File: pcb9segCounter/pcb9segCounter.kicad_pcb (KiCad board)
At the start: 2 copper layers, 10 parts

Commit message: Making progress, figuring out microcontroller interfacing
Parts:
- removed the D1 at (148.2, 54.6)
- added C1: 0.1u, Capacitor_SMD:C_0805_2012Metric, F.Cu at (64.0, 142.5)
- added D10: ~, customParts:1x1mm SMD RGB LED, F.Cu at (103.6, 49.3)
- added D11: ~, customParts:1x1mm SMD RGB LED, F.Cu at (115.5, 60.0)
- added D12: ~, customParts:1x1mm SMD RGB LED, F.Cu at (117.6, 79.1)
- added D13: ~, customParts:1x1mm SMD RGB LED, F.Cu at (107.3, 90.8)
- added D14: ~, customParts:1x1mm SMD RGB LED, F.Cu at (94.8, 80.1)
- added D15: ~, customParts:1x1mm SMD RGB LED, F.Cu at (92.8, 60.7)
- added D16: ~, customParts:1x1mm SMD RGB LED, F.Cu at (100.7, 62.5)
- added D17: ~, customParts:1x1mm SMD RGB LED, F.Cu at (103.3, 67.2)
- added D18: ~, customParts:1x1mm SMD RGB LED, F.Cu at (103.6, 80.3)
- added D19: ~, customParts:1x1mm SMD RGB LED, F.Cu at (131.5, 49.3)
- added D20: ~, customParts:1x1mm SMD RGB LED, F.Cu at (143.4, 60.0)
- added D21: ~, customParts:1x1mm SMD RGB LED, F.Cu at (145.6, 79.1)
- added D22: ~, customParts:1x1mm SMD RGB LED, F.Cu at (135.2, 90.8)
- added D23: ~, customParts:1x1mm SMD RGB LED, F.Cu at (122.7, 80.1)
- added D24: ~, customParts:1x1mm SMD RGB LED, F.Cu at (120.8, 60.7)
- added D25: ~, customParts:1x1mm SMD RGB LED, F.Cu at (128.7, 62.5)
- added D26: ~, customParts:1x1mm SMD RGB LED, F.Cu at (131.2, 67.2)
- added D27: ~, customParts:1x1mm SMD RGB LED, F.Cu at (131.5, 80.3)
- added D28: ~, customParts:1x1mm SMD RGB LED, F.Cu at (159.4, 49.3)
- added D29: ~, customParts:1x1mm SMD RGB LED, F.Cu at (171.4, 60.0)
- added D30: ~, customParts:1x1mm SMD RGB LED, F.Cu at (173.5, 79.1)
- added D31: ~, customParts:1x1mm SMD RGB LED, F.Cu at (163.2, 90.8)
- added D32: ~, customParts:1x1mm SMD RGB LED, F.Cu at (150.7, 80.1)
- added D33: ~, customParts:1x1mm SMD RGB LED, F.Cu at (148.7, 60.7)
- added D34: ~, customParts:1x1mm SMD RGB LED, F.Cu at (156.6, 62.5)
- added D35: ~, customParts:1x1mm SMD RGB LED, F.Cu at (159.1, 67.2)
- added D36: ~, customParts:1x1mm SMD RGB LED, F.Cu at (159.4, 80.3)
- added J1: SAO, Connector_PinHeader_2.54mm:PinHeader_2x03_P2.54mm_Vertical, F.Cu at (73.3, 130.7)
- added J2: AVR-ISP-6, Connector_PinHeader_2.54mm:PinHeader_2x03_P2.54mm_Vertical, F.Cu at (64.1, 130.7)
- added R1: 1k, Resistor_SMD:R_0805_2012Metric_Pad1.20x1.40mm_HandSolder, F.Cu at (64.1, 139.5)
- added R2: 1k, Resistor_SMD:R_0805_2012Metric, F.Cu at (55.5, 140.2)
- added R3: 1k, Resistor_SMD:R_0805_2012Metric, F.Cu at (55.5, 143.1)
- added S1: ~, customParts:9 Segment 38x19x3, B.Cu at (88.9, 50.8)
- added S2: ~, customParts:9 Segment 38x19x3, B.Cu at (116.8, 50.8)
- added S3: ~, customParts:9 Segment 38x19x3, B.Cu at (144.8, 50.8)
- added S4: ~, customParts:9 Segment 38x19x3, B.Cu at (172.7, 50.8)
- added U1: ATtiny84A-SS, Package_SO:SOIC-14_3.9x8.7mm_P1.27mm, F.Cu at (57.5, 133.6)
- moved D7 60.3 mm to (72.8, 62.5)
- moved D8 60.2 mm to (75.3, 67.2)
- moved D4 59.4 mm to (79.3, 90.8)
- moved D2 59.4 mm to (87.5, 60.0)
- moved D5 59.4 mm to (66.9, 80.1)
- moved D1 59.4 mm to (75.6, 49.3)
- moved D3 59.4 mm to (89.7, 79.1)
- moved D6 59.4 mm to (64.9, 60.7)
- moved D9 59.4 mm to (75.6, 80.3)
- renumbered D2 to D1, D3 to D2, D4 to D3, D5 to D4, D6 to D5, D7 to D6, D8 to D7, D9 to D8, D10 to D9
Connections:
- net /pcb9SegDigit/pwr+ renamed +5V
- net /pcb9SegDigit/pwr- renamed GND
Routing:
- net GND: track 79.1 -> 646.1 mm
- net +5V: track 73.7 -> 606.5 mm
- net /pcb9SegDigit2/DOUT: track 0.00 -> 68.7 mm, vias 0 -> 2
- net /pcb9SegDigit1/DOUT: track 0.00 -> 68.7 mm, vias 0 -> 2
- net /pcb9SegDigit/DOUT: track 0.00 -> 68.7 mm, vias 0 -> 2
- net Net-(D15-DOUT): track 0.00 -> 26.3 mm
- net Net-(D24-DOUT): track 0.00 -> 26.3 mm
- net Net-(D33-DOUT): track 0.00 -> 26.3 mm
- net Net-(D21-DOUT): track 0.00 -> 20.2 mm
- net Net-(D12-DOUT): track 0.00 -> 20.2 mm
- net Net-(D30-DOUT): track 0.00 -> 20.2 mm
- net Net-(D3-DOUT): track 0.00 -> 20.2 mm
- net Net-(D28-DOUT): track 0.00 -> 19.4 mm
- net Net-(D19-DOUT): track 0.00 -> 19.4 mm
- net Net-(D10-DOUT): track 0.00 -> 19.4 mm
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
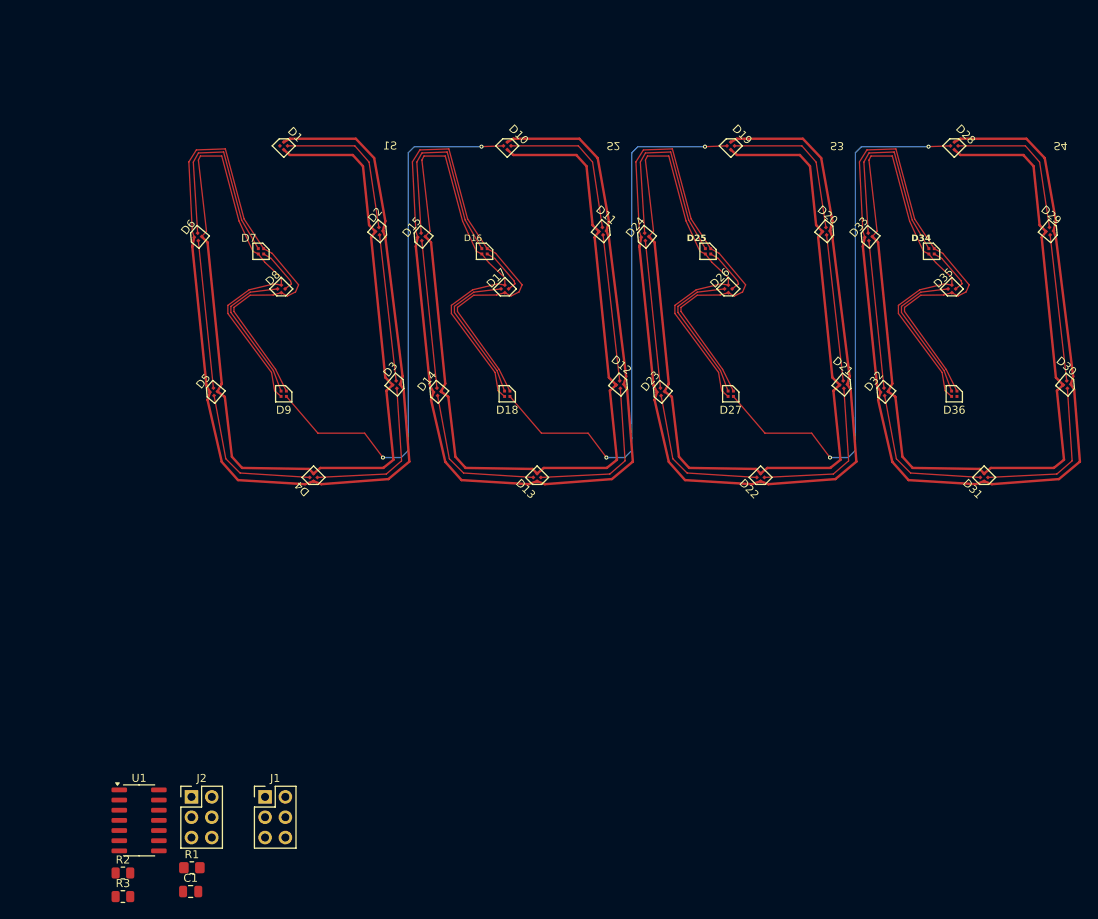
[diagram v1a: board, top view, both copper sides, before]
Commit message: Schematic looks good, going to branch to reduce the number of digits from 4 to 2
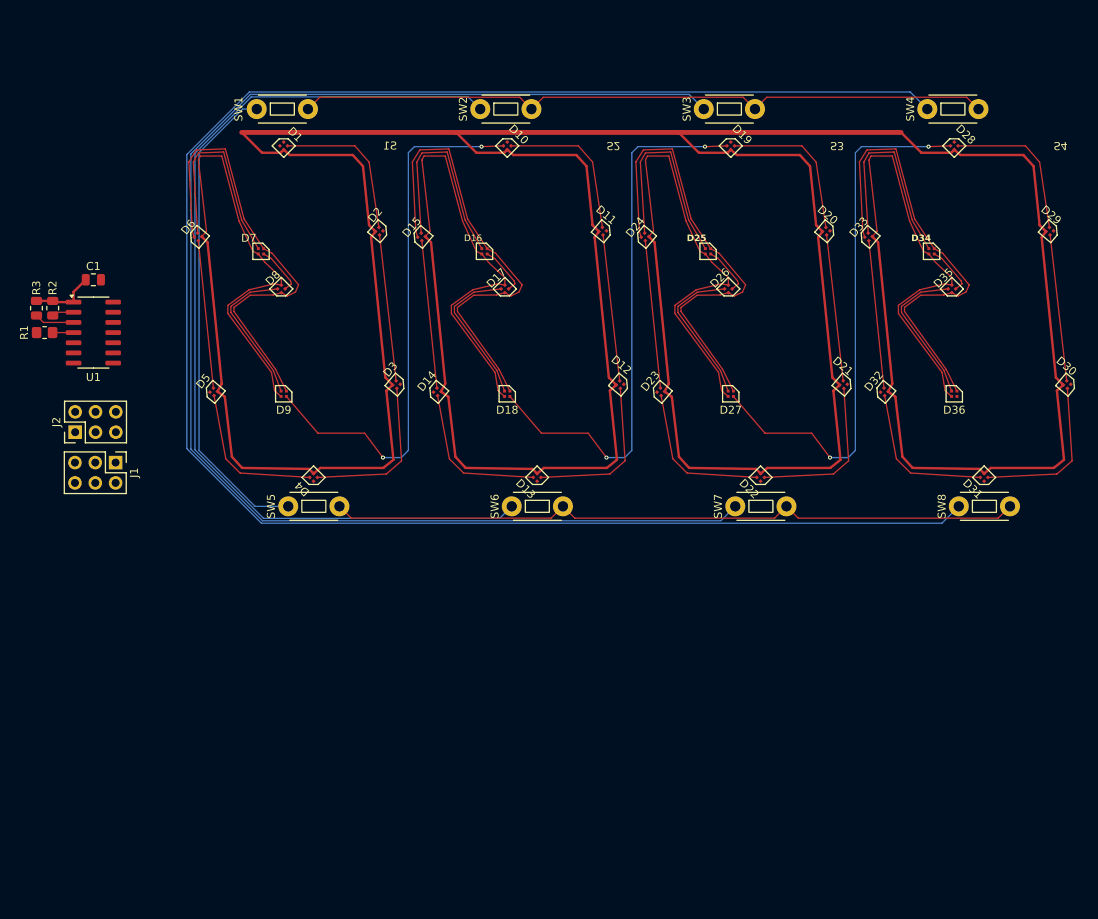
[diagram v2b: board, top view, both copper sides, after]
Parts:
- added SW1: ~, customParts:PTS636 SK43 LFS, F.Cu at (75.4, 44.7)
- added SW2: ~, customParts:PTS636 SK43 LFS, F.Cu at (103.4, 44.7)
- added SW3: ~, customParts:PTS636 SK43 LFS, F.Cu at (131.3, 44.7)
- added SW4: ~, customParts:PTS636 SK43 LFS, F.Cu at (159.3, 44.7)
- added SW5: ~, customParts:PTS636 SK43 LFS, F.Cu at (79.4, 94.4)
- added SW6: ~, customParts:PTS636 SK43 LFS, F.Cu at (107.3, 94.4)
- added SW7: ~, customParts:PTS636 SK43 LFS, F.Cu at (135.3, 94.4)
- added SW8: ~, customParts:PTS636 SK43 LFS, F.Cu at (163.2, 94.4)
- moved C1 77.4 mm to (51.8, 66.0)
- moved R3 74.3 mm to (44.7, 69.6), turned to -90 degrees
- moved R2 71.1 mm to (46.7, 69.6), turned to -90 degrees
- moved R1 69.4 mm to (45.7, 72.6)
- moved U1 61.2 mm to (51.8, 72.6)
- moved J2 47.8 mm to (49.5, 85.1), turned to 90 degrees
- moved J1 45.8 mm to (54.6, 88.9), turned to -90 degrees
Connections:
- J2 pad 3: /uC/SCK -> SCL
- J2 pad 4: /uC/MOSI -> SDA
- U1 pad 6: unconnected-(U1-PA7-Pad6) -> GP1
- U1 pad 7: /uC/MOSI -> SDA
- U1 pad 9: /uC/SCK -> SCL
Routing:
- net GND: track 646.1 -> 226.5 mm
- net /uC/tho: track 0.00 -> 234.7 mm
- net /uC/hnd: track 0.00 -> 177.4 mm
- net +5V: track 606.5 -> 726.7 mm
- net /uC/ten: track 0.00 -> 120.0 mm
- net /uC/dec: track 0.00 -> 92.5 mm
- net /uC/inc: track 0.00 -> 90.3 mm
- net /uC/one: track 0.00 -> 60.7 mm
- net /uC/RST: track 0.00 -> 2.62 mm

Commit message: reduced to 2 digits, added capacitors
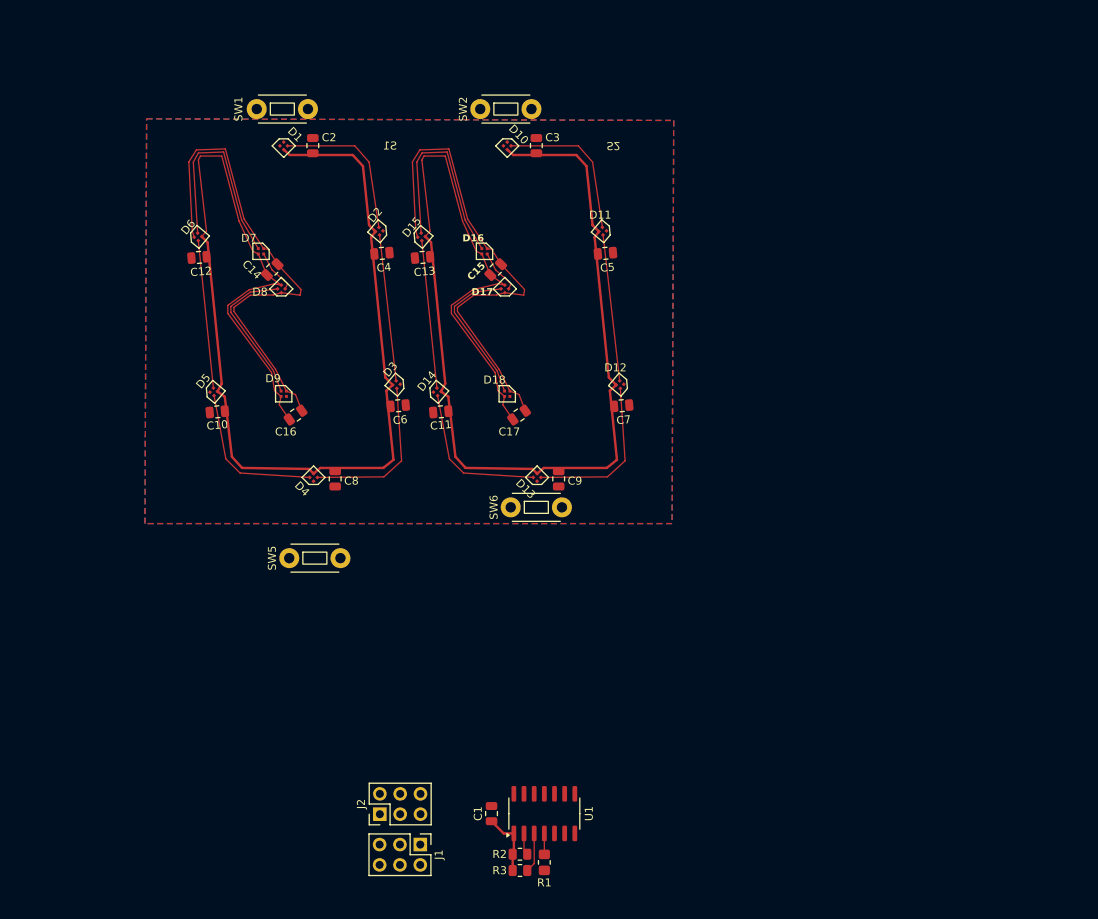
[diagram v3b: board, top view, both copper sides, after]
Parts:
- removed D19, D20, D21, D22, D23, D24, D25, D26, D27, D28, D29, D30, D31, D32, D33, D34, D35, D36: ~, customParts:1x1mm SMD RGB LED
- removed S3, S4: ~, customParts:9 Segment 38x19x3
- removed SW3, SW4, SW7, SW8: ~, customParts:PTS636 SK43 LFS
- added C10: 0.1u, Capacitor_SMD:C_0805_2012Metric, F.Cu at (67.3, 82.5)
- added C11: 0.1u, Capacitor_SMD:C_0805_2012Metric, F.Cu at (95.3, 82.5)
- added C12: 0.1u, Capacitor_SMD:C_0805_2012Metric, F.Cu at (65.0, 63.2)
- added C13: 0.1u, Capacitor_SMD:C_0805_2012Metric, F.Cu at (93.0, 63.2)
- added C14: 0.1u, Capacitor_SMD:C_0805_2012Metric, F.Cu at (74.2, 64.8)
- added C15: 0.1u, Capacitor_SMD:C_0805_2012Metric, F.Cu at (102.1, 64.8)
- added C16: 0.1u, Capacitor_SMD:C_0805_2012Metric, F.Cu at (77.1, 83.0)
- added C17: 0.1u, Capacitor_SMD:C_0805_2012Metric, F.Cu at (105.0, 83.0)
- added C2: 0.1u, Capacitor_SMD:C_0805_2012Metric, F.Cu at (79.2, 49.3)
- added C3: 0.1u, Capacitor_SMD:C_0805_2012Metric, F.Cu at (107.2, 49.3)
- added C4: 0.1u, Capacitor_SMD:C_0805_2012Metric, F.Cu at (87.9, 62.7)
- added C5: 0.1u, Capacitor_SMD:C_0805_2012Metric, F.Cu at (115.8, 62.7)
- added C6: 0.1u, Capacitor_SMD:C_0805_2012Metric, F.Cu at (89.9, 81.8)
- added C7: 0.1u, Capacitor_SMD:C_0805_2012Metric, F.Cu at (117.9, 81.8)
- added C8: 0.1u, Capacitor_SMD:C_0805_2012Metric, F.Cu at (82.0, 90.9)
- added C9: 0.1u, Capacitor_SMD:C_0805_2012Metric, F.Cu at (110.0, 90.9)
- moved R3 92.7 mm to (105.1, 139.9), turned to 0 degrees
- moved R1 91.0 mm to (108.2, 138.9), turned to 90 degrees
- moved R2 89.8 mm to (105.1, 137.9), turned to 0 degrees
- moved C1 83.2 mm to (101.6, 132.8), turned to 90 degrees
- moved U1 82.4 mm to (108.2, 132.8), turned to 90 degrees
- moved J1 61.1 mm to (92.7, 136.6)
- moved J2 61.1 mm to (87.6, 132.8)
- moved SW5 6.48 mm to (79.5, 100.8)
- moved SW6 0.18 mm to (107.2, 94.5)
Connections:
- D1 pad 2: /pcb9SegDigit/DIN -> GP2
- U1 pad 10: /uC/tho -> unconnected-(U1-PA3-Pad10)
- U1 pad 11: /uC/hnd -> unconnected-(U1-PA2-Pad11)
- U1 pad 5: /pcb9SegDigit/DIN -> GP2
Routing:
- net +5V: track 726.7 -> 317.9 mm
- net /uC/tho: track 234.7 -> 0.00 mm
- net /uC/hnd: track 177.4 -> 0.00 mm
- net /uC/ten: track 120.0 -> 0.00 mm
- net GND: track 226.5 -> 121.7 mm
- net /uC/dec: track 92.5 -> 5.00 mm
- net /uC/inc: track 90.3 -> 2.77 mm
- net /pcb9SegDigit2/DOUT: track 68.7 -> 0.00 mm, vias 2 -> 0
- net /pcb9SegDigit1/DOUT: track 68.7 -> 0.00 mm, vias 2 -> 0
- net /pcb9SegDigit/DOUT: track 68.7 -> 0.00 mm, vias 2 -> 0
- net /uC/one: track 60.7 -> 0.00 mm
- net Net-(D24-DOUT): track 26.3 -> 0.00 mm
- net Net-(D33-DOUT): track 26.3 -> 0.00 mm
- net Net-(D21-DOUT): track 20.2 -> 0.00 mm
- net Net-(D30-DOUT): track 20.2 -> 0.00 mm
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- added copper zone on B.Cu, net (none)
- added copper zone on F.Cu, net GND

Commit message: Edits prior to setting board edge in freecad
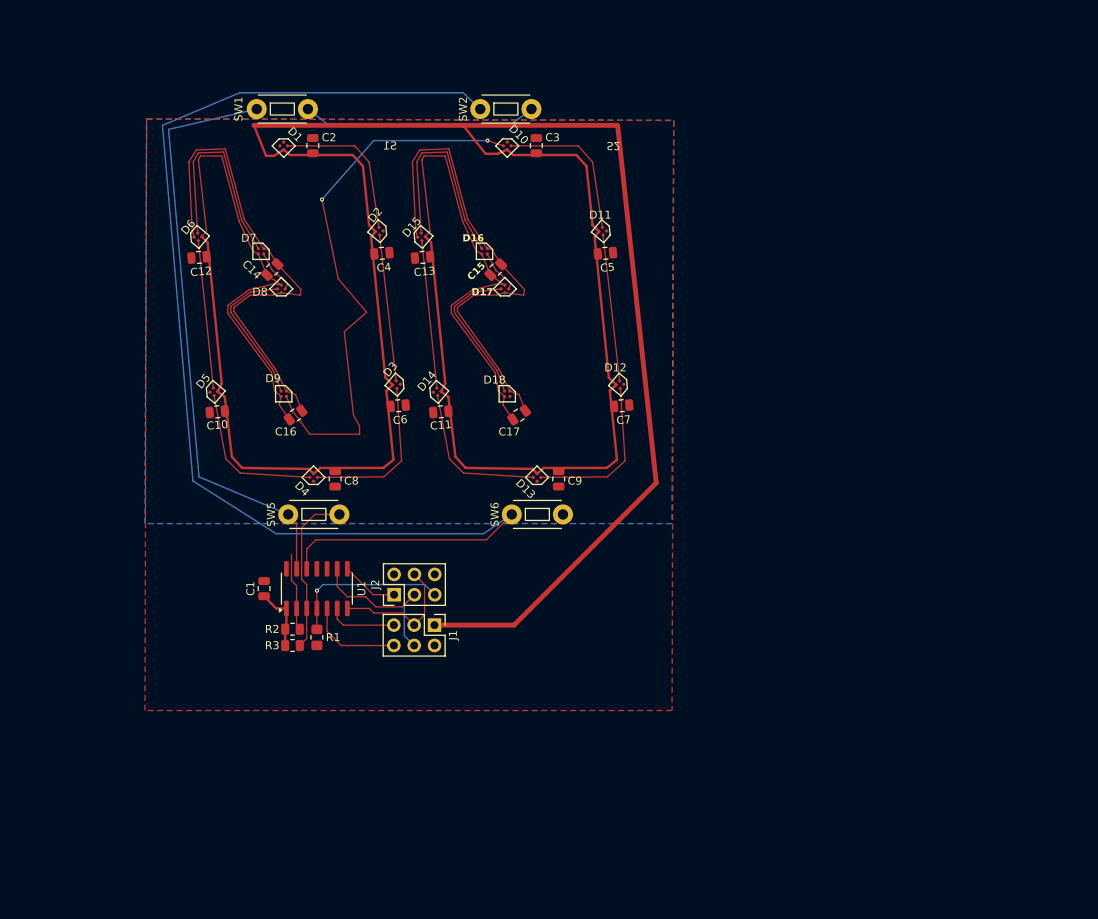
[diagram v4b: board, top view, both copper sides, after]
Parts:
- moved R2 40.0 mm to (76.7, 109.7)
- moved C1 40.0 mm to (73.2, 104.6)
- moved R1 40.0 mm to (79.8, 110.7)
- moved R3 40.0 mm to (76.7, 111.8)
- moved U1 40.0 mm to (79.8, 104.6)
- moved J2 27.5 mm to (89.4, 105.4)
- moved J1 27.5 mm to (94.5, 109.2)
- moved SW5 5.46 mm to (79.4, 95.4)
- moved SW6 0.90 mm to (107.3, 95.4)
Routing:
- net /uC/ten: track 0.00 -> 158.4 mm
- net +5V: track 317.9 -> 457.3 mm
- net /uC/one: track 0.00 -> 74.2 mm
- net /pcb9SegDigit/DOUT: track 0.00 -> 70.3 mm, vias 0 -> 2
- net /uC/inc: track 2.77 -> 39.1 mm
- net SCL: track 0.00 -> 20.9 mm
- net /uC/RST: track 2.62 -> 20.4 mm, vias 0 -> 1
- net SDA: track 0.00 -> 16.6 mm
- net /uC/dec: track 5.00 -> 20.8 mm
- net GP2: track 0.00 -> 12.0 mm
- net GP1: track 0.00 -> 8.74 mm
- net /uC/MISO: track 0.00 -> 7.18 mm

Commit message: good routing, need to add slikscreen details
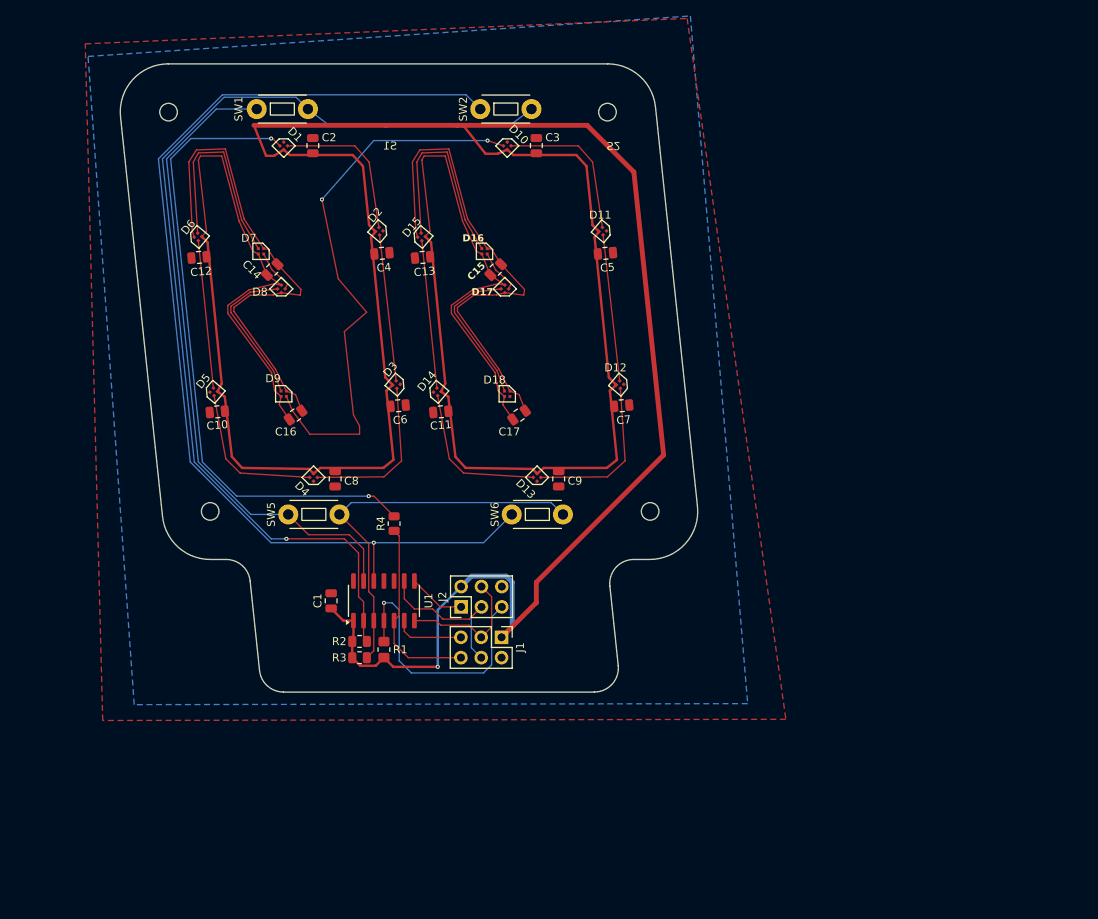
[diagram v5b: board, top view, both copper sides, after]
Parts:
- added H1: ~, MountingHole:MountingHole_2.2mm_M2_ISO7380, F.Cu at (61.2, 45.1)
- added H2: ~, MountingHole:MountingHole_2.2mm_M2_ISO7380, F.Cu at (116.1, 45.1)
- added H3: ~, MountingHole:MountingHole_2.2mm_M2_ISO7380, F.Cu at (66.4, 95.0)
- added H4: ~, MountingHole:MountingHole_2.2mm_M2_ISO7380, F.Cu at (121.4, 95.0)
- added R4: 500, Resistor_SMD:R_0805_2012Metric, F.Cu at (89.4, 96.5)
- moved C1 8.52 mm to (81.5, 106.2)
- moved J1 8.52 mm to (102.8, 110.7)
- moved J2 8.52 mm to (97.8, 106.9)
- moved R1 8.52 mm to (88.1, 112.3)
- moved R2 8.52 mm to (85.1, 111.3)
- moved R3 8.52 mm to (85.1, 113.3)
- moved U1 8.52 mm to (88.1, 106.2)
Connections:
- D1 pad 2: GP2 -> /pcb9SegDigit/DIN
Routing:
- net /uC/ten: track 158.4 -> 94.9 mm, vias 0 -> 1
- net /uC/inc: track 39.1 -> 88.0 mm, vias 0 -> 1
- net /pcb9SegDigit/DIN: track 0.00 -> 41.9 mm, vias 0 -> 2
- net /uC/one: track 74.2 -> 43.0 mm
- net /uC/dec: track 20.8 -> 49.2 mm
- net /uC/RST: track 20.4 -> 33.8 mm
- net GP2: track 12.0 -> 23.7 mm
- net +5V: track 457.3 -> 450.8 mm, vias 0 -> 1
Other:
- board outline added: 72.2 x 78.5 mm
